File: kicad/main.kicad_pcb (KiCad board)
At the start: 2 copper layers, 130.7 x 94.9 mm, 40 parts

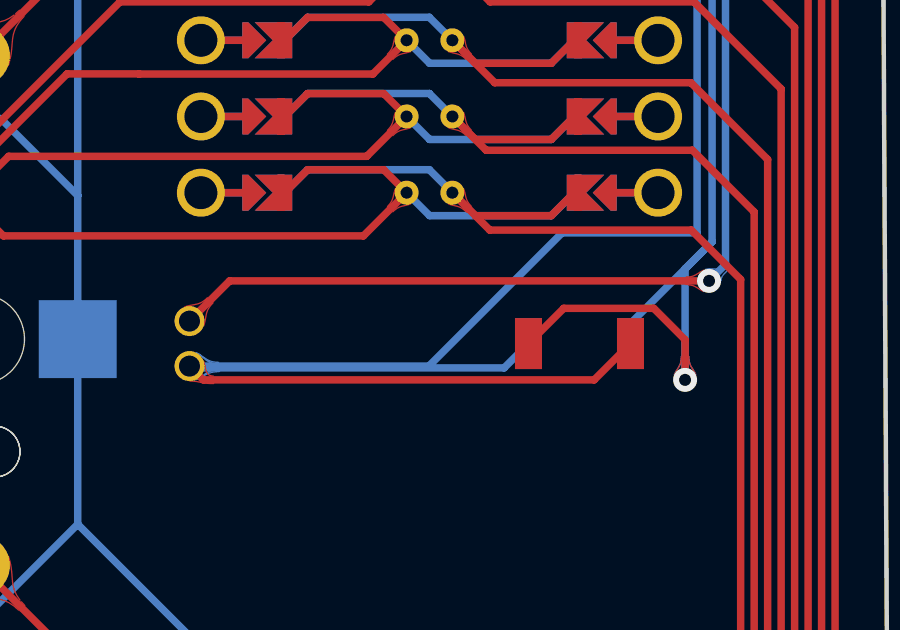
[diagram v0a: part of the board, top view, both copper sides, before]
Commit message: fix: reset button placement
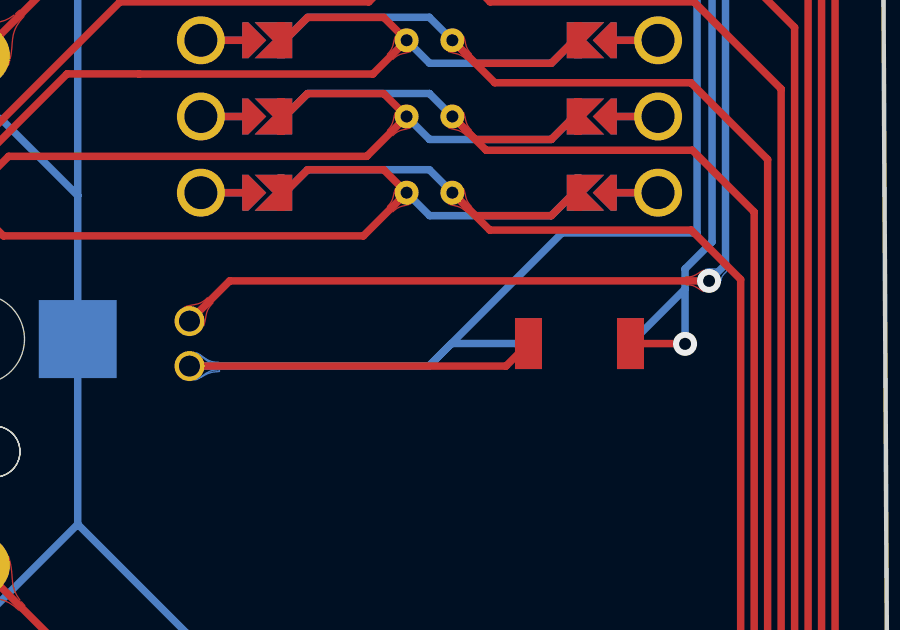
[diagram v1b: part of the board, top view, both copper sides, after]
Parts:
- turned ? to 0 degrees
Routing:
- net GND: track 959.2 -> 947.4 mm
- net RST: track 50.8 -> 42.7 mm

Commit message: chore: regenerate teardrops
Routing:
- net P10: track 81.1 -> 81.8 mm
